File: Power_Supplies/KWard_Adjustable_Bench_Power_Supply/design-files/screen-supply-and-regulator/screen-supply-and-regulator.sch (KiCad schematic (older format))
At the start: 35 parts, among them J1 120VAC, J2 Tube Pass Array, J3 To B+ current/volt meters, J4 To Panel Jacks, Q1 STP16N50M2, SW1 I-meter bypass, SW2 DUT discharge, U1 LM317_TO-220

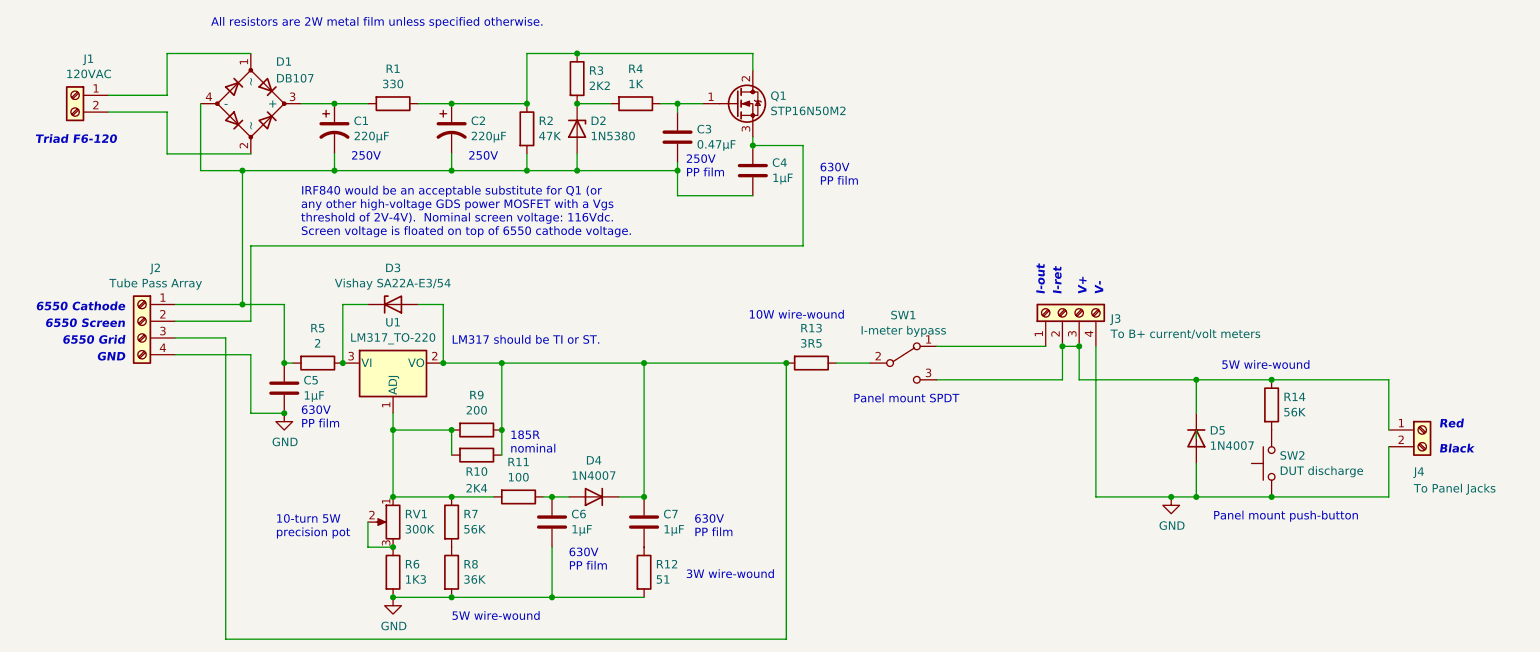
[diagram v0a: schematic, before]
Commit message: Minor tweaks to the silk screen on the regulator board.
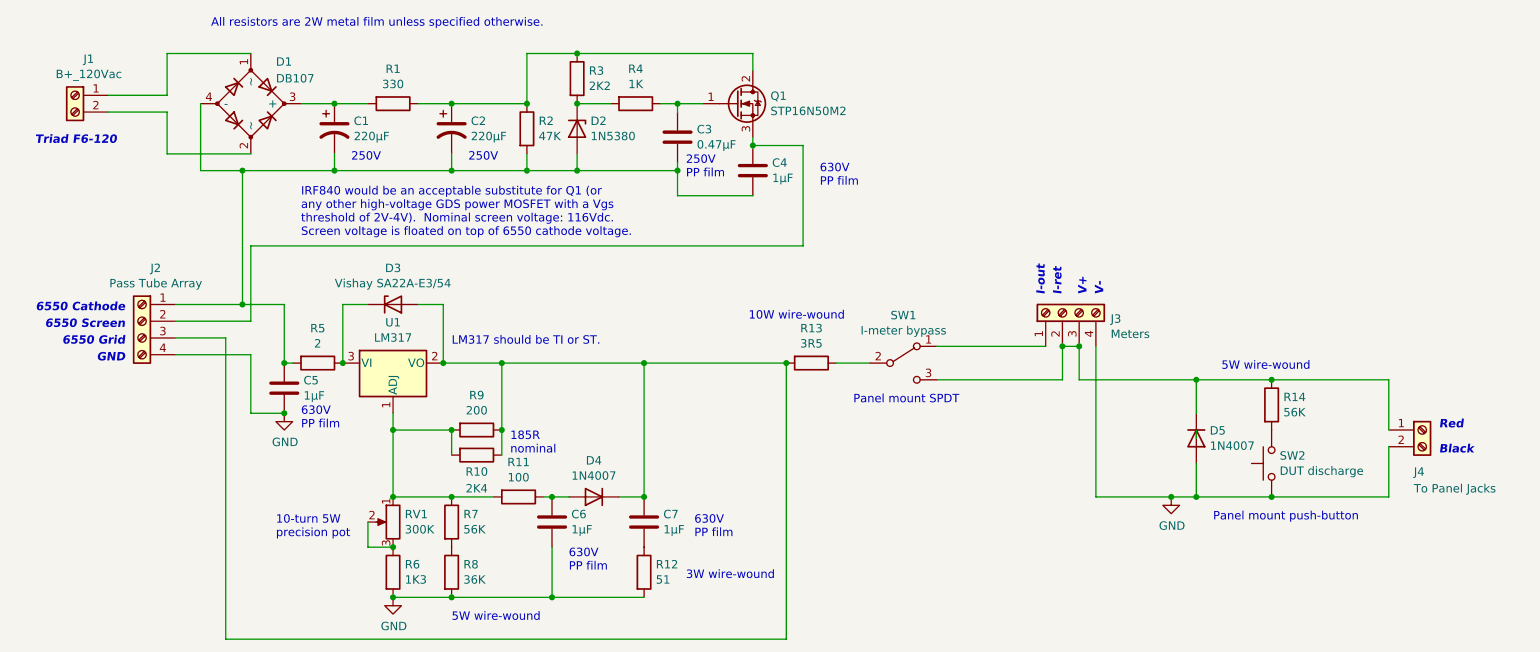
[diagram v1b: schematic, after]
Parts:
- J1: value 120VAC -> B+_120Vac
- J2: value Tube Pass Array -> Pass Tube Array
- J3: value To B+ current/volt meters -> Meters
- U1: value LM317_TO-220 -> LM317
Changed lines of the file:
@@
 P 1250 2500
 F 0 "J1" H 1168 2717 50  0000 C CNN
-F 1 "120VAC" H 1168 2626 50  0000 C CNN
+F 1 "B+_120Vac" H 1168 2626 50  0000 C CNN
 F 2 "TerminalBlock:TerminalBlock_bornier-2_P5.08mm" H 1250 2500 50  0001 C CNN
 F 3 "~" H 1250 2500 50  0001 C CNN
@@
 P 3150 4100
 F 0 "U1" H 3150 4342 50  0000 C CNN
-F 1 "LM317_TO-220" H 3150 4251 50  0000 C CNN
+F 1 "LM317" H 3150 4251 50  0000 C CNN
 F 2 "Package_TO_SOT_THT:TO-220-3_Vertical" H 3150 4350 50  0001 C CIN
 F 3 "http://www.ti.com/lit/ds/symlink/lm317.pdf" H 3150 4100 50  0001 C CNN
@@
 P 7150 3800
 F 0 "J3" V 7114 3512 50  0000 R CNN
-F 1 "To B+ current/volt meters" V 7023 3512 50  0000 R CNN
+F 1 "Meters" V 7023 3512 50  0000 R CNN
 F 2 "jrt-TerminalBlocks:TE_AMP-4_P10.16mm" H 7150 3800 50  0001 C CNN
 F 3 "~" H 7150 3800 50  0001 C CNN
@@
 P 1650 3850
 F 0 "J2" H 1568 4167 50  0000 C CNN
-F 1 "Tube Pass Array" H 1568 4076 50  0000 C CNN
+F 1 "Pass Tube Array" H 1568 4076 50  0000 C CNN
 F 2 "jrt-TerminalBlocks:TE_AMP-4_P10.16mm" H 1650 3850 50  0001 C CNN
 F 3 "~" H 1650 3850 50  0001 C CNN

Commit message: Part # tweaks (to reflect currently-available components).
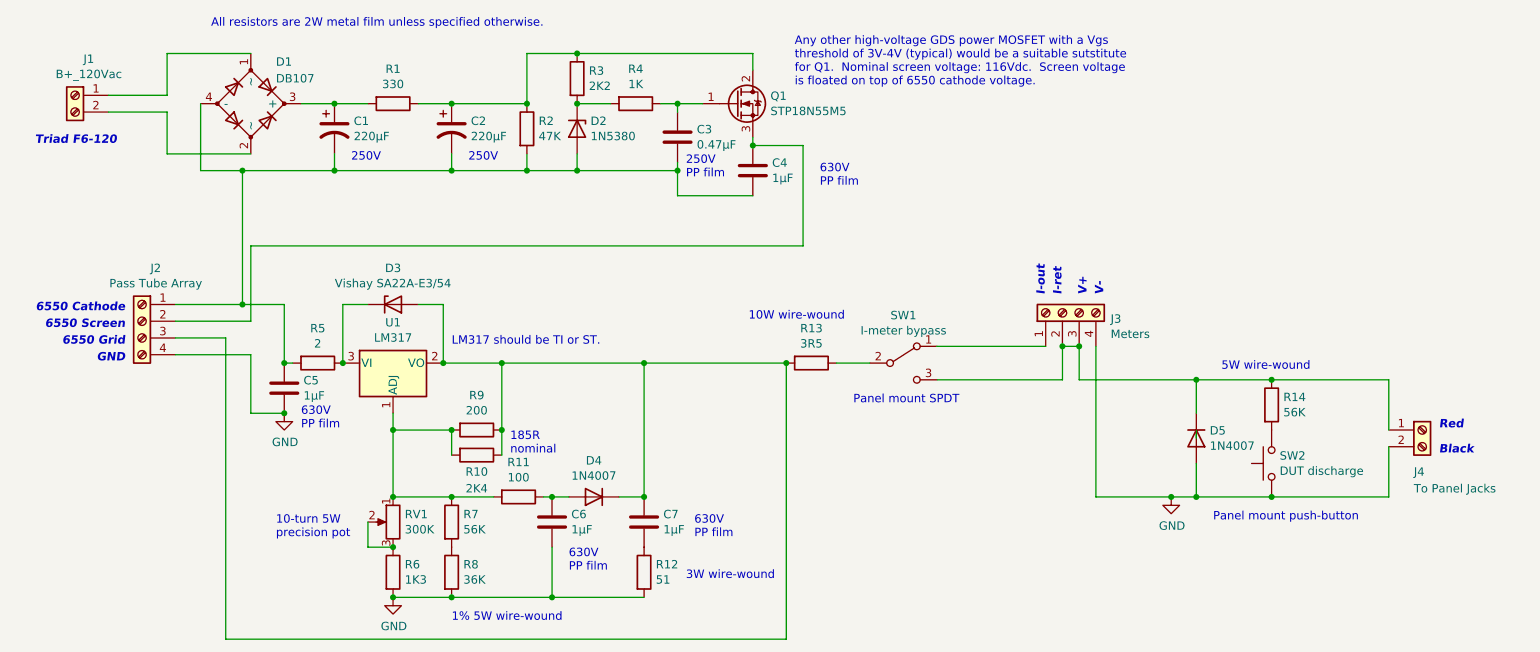
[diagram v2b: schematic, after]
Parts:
- Q1: value STP16N50M2 -> STP18N55M5
- R8: Mouser 71-CW00536K00JE73 -> 71-RS00236K00FB12
- U1: Mouser (none) -> 926-LM317AT/NOPB
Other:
- note added: "1% 5W wire-wound"
- note added: "Any other high-voltage GDS power MOSFET with a Vgs\nthreshold of 3V-4V (typical) would be a suitable sutstitute\nfor Q1. Nominal screen voltage: 116Vdc. Screen voltage\nis floated on top of 6550 cathode voltage."
- note removed: "IRF840 would be an acceptable substitute for Q1 (or\nany other high-voltage GDS power MOSFET with a Vgs\nthreshold of 2V-4V). Nominal screen voltage: 116Vdc.\nScreen voltage is floated on top of 6550 cathode voltage."
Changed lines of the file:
@@
 P 5200 2550
 F 0 "Q1" H 5405 2596 50  0000 L CNN
-F 1 "STP16N50M2" H 5405 2505 50  0000 L CNN
+F 1 "STP18N55M5" H 5405 2505 50  0000 L CNN
 F 2 "Package_TO_SOT_THT:TO-220-3_Vertical" H 5400 2650 50  0001 C CNN
 F 3 "~" H 5200 2550 50  0001 C CNN
@@
 Wire Wire Line
 	4850 3100 5300 3100
-Text Notes 2600 3350 0    50   ~ 0
-IRF840 would be an acceptable substitute for Q1 (or\nany other high-voltage GDS power MOSFET with a Vgs\nthreshold of 2V-4V).  Nominal screen voltage: 116Vdc.\nScreen voltage is floated on top of 6550 cathode voltage.
+Text Notes 5550 2450 0    50   ~ 0
+Any other high-voltage GDS power MOSFET with a Vgs\nthreshold of 3V-4V (typical) would be a suitable sutstitute\nfor Q1.  Nominal screen voltage: 116Vdc.  Screen voltage\nis floated on top of 6550 cathode voltage.
 Wire Wire Line
 	4250 2550 4450 2550
@@
 F 2 "Package_TO_SOT_THT:TO-220-3_Vertical" H 3150 4350 50  0001 C CIN
 F 3 "http://www.ti.com/lit/ds/symlink/lm317.pdf" H 3150 4100 50  0001 C CNN
+F 4 "926-LM317AT/NOPB" H 3150 4100 50  0001 C CNN "Mouser"
 	1    3150 4100
 	1    0    0    -1
@@
 F 2 "Resistor_THT:R_Axial_Power_L25.0mm_W9.0mm_P30.48mm" V 3430 5350 50  0001 C CNN
 F 3 "~" H 3500 5350 50  0001 C CNN
-F 4 "71-CW00536K00JE73" H 3500 5350 50  0001 C CNN "Mouser"
+F 4 "71-RS00236K00FB12" H 3500 5350 50  0001 C CNN "Mouser"
 	1    3500 5350
 	1    0    0    -1
@@
 3W wire-wound
 Text Notes 3500 5650 0    50   ~ 0
-5W wire-wound
+1% 5W wire-wound
 Wire Wire Line
 	4100 4900 4200 4900
